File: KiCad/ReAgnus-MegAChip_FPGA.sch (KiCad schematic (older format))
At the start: 2 parts, among them U7 GW1N-UV9LQ144

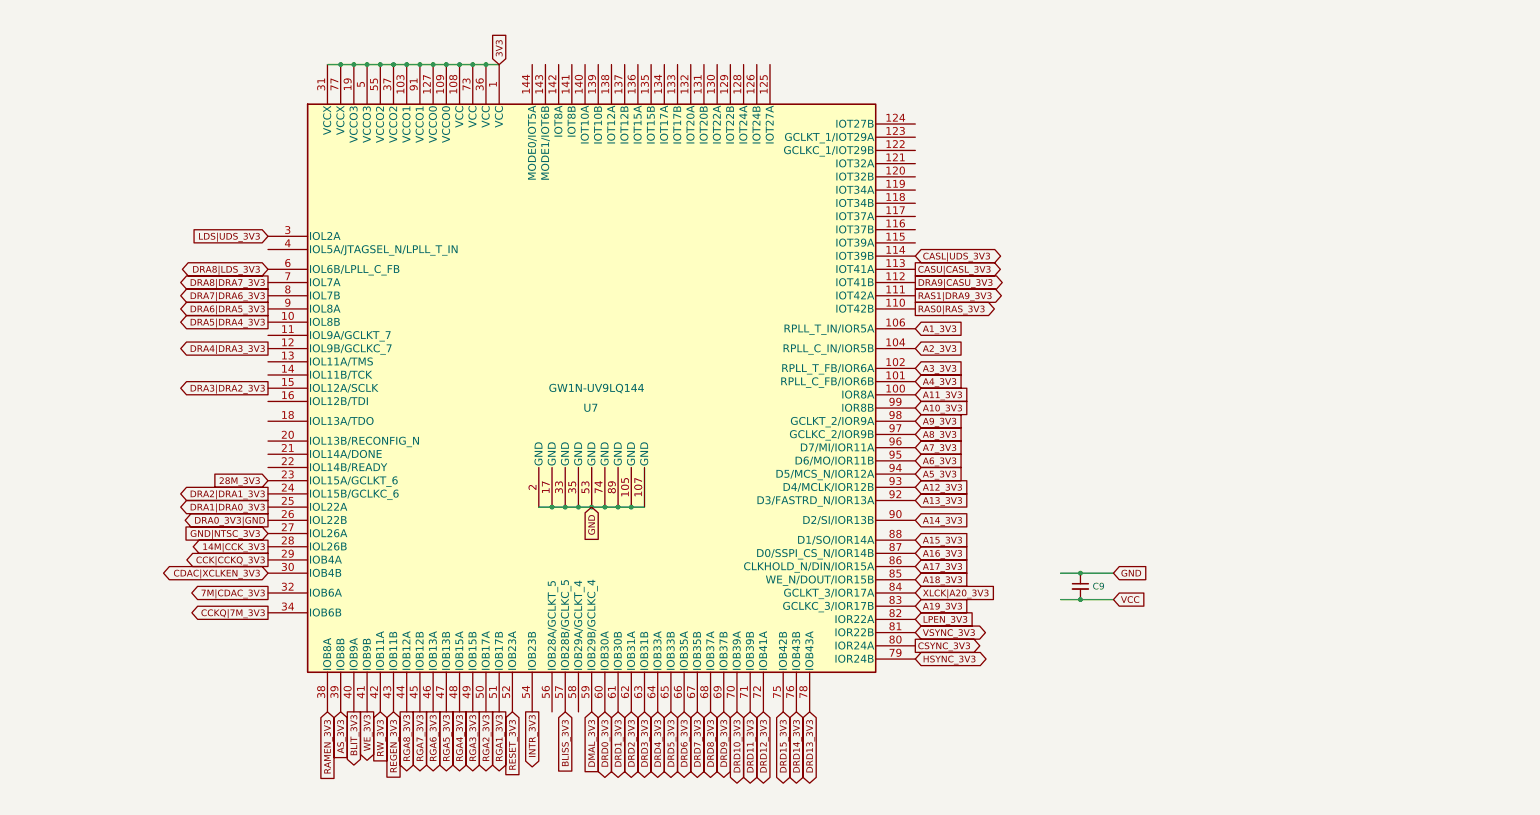
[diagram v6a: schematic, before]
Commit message: added pull-up resistors on PAL/NTSC-line, added JTAG-header
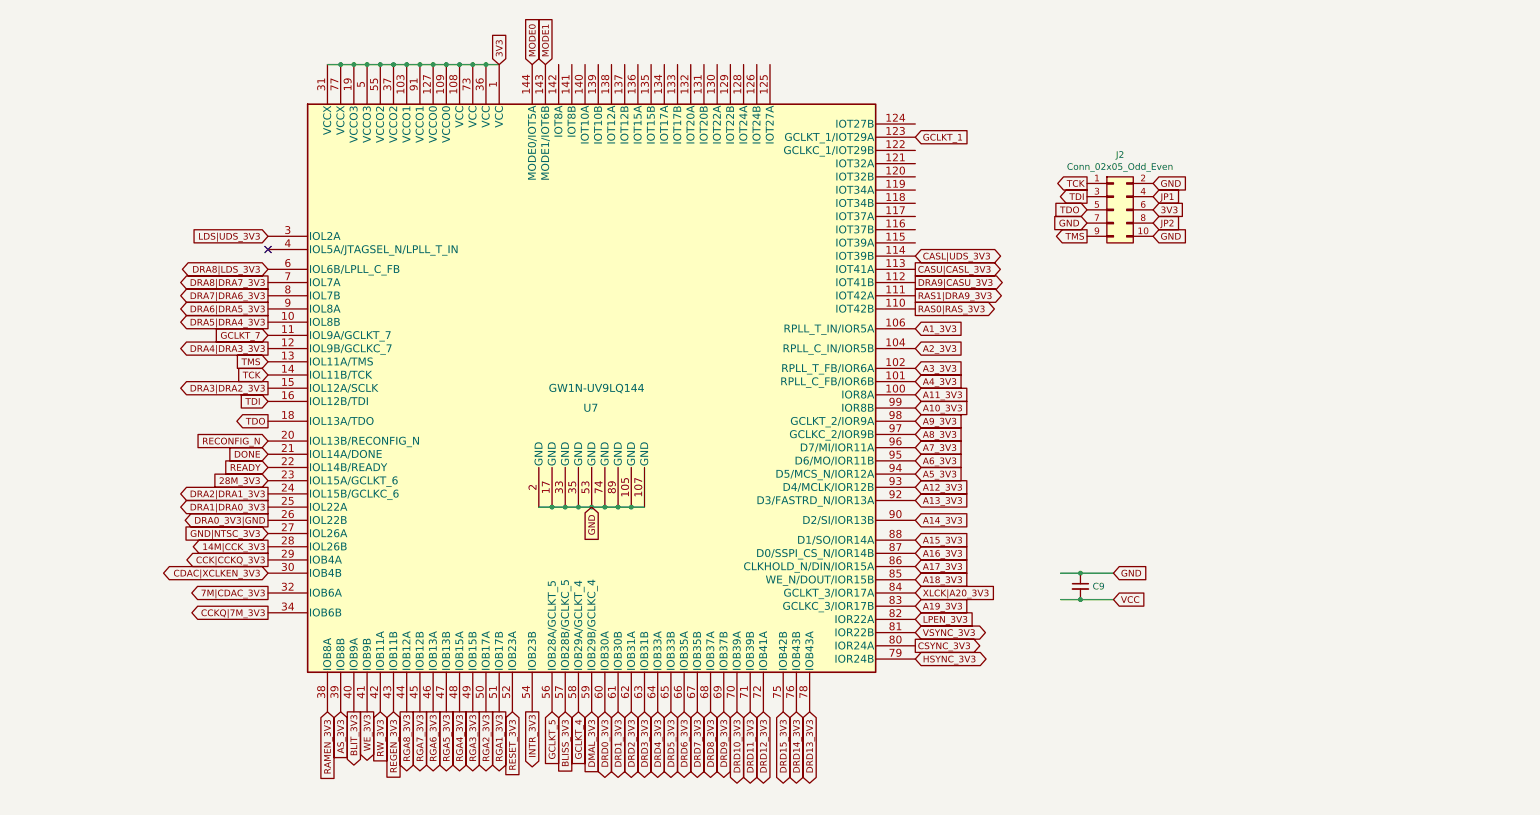
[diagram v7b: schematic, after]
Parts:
- added J2: Conn_02x05_Odd_Even, Connector_PinHeader_2.54mm:PinHeader_2x05_P2.54mm_Vertical, symbol Connector_Generic:Conn_02x05_Odd_Even
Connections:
- net labels added: DONE, GCLKT_1, GCLKT_4, GCLKT_5, GCLKT_7, JP1, JP2, MODE0, MODE1, READY, RECONFIG_N, TCK, TDI, TDO, TMS
- no-connect marks 0 -> 1
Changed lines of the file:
@@
 Text GLabel 3700 5950 3    50   Input ~ 0
 BLISS_3V3
+$Comp
+L Connector_Generic:Conn_02x05_Odd_Even J2
+U 1 1 6329A00B
+P 7850 2150
+F 0 "J2" H 7900 2567 50  0000 C CNN
+F 1 "Conn_02x05_Odd_Even" H 7900 2476 50  0000 C CNN
+F 2 "Connector_PinHeader_2.54mm:PinHeader_2x05_P2.54mm_Vertical" H 7850 2150 50  0001 C CNN
+F 3 "~" H 7850 2150 50  0001 C CNN
+	1    7850 2150
+	1    0    0    -1
+$EndComp
+Text GLabel 7650 1950 0    50   Output ~ 0
+TCK
+Text GLabel 7650 2050 0    50   Output ~ 0
+TDI
+Text GLabel 7650 2150 0    50   Input ~ 0
+TDO
+Text GLabel 7650 2250 0    50   Input ~ 0
+GND
+Text GLabel 7650 2350 0    50   Output ~ 0
+TMS
+Text GLabel 8150 1950 2    50   Input ~ 0
+GND
+Text GLabel 8150 2350 2    50   Input ~ 0
+GND
+Text GLabel 8150 2050 2    50   Input ~ 0
+JP1
+Text GLabel 8150 2250 2    50   Input ~ 0
+JP2
+Text GLabel 8150 2150 2    50   Input ~ 0
+3V3
+Text GLabel 1450 3400 0    50   Input ~ 0
+TCK
+Text GLabel 1450 3600 0    50   Input ~ 0
+TDI
+Text GLabel 1450 3750 0    50   Output ~ 0
+TDO
+Text GLabel 1450 3300 0    50   Input ~ 0
+TMS
+Text GLabel 1450 3900 0    50   Input ~ 0
+RECONFIG_N
+Text GLabel 1450 4000 0    50   Input ~ 0
+DONE
+Text GLabel 1450 4100 0    50   Input ~ 0
+READY
+Text GLabel 1450 3100 0    50   Input ~ 0
+GCLKT_7
+Text GLabel 3600 5950 3    50   Input ~ 0
+GCLKT_5
+Text GLabel 3800 5950 3    50   Input ~ 0
+GCLKT_4
+Text GLabel 6350 1600 2    50   Input ~ 0
+GCLKT_1
+Text GLabel 3550 1050 1    50   Input ~ 0
+MODE1
+Text GLabel 3450 1050 1    50   Input ~ 0
+MODE0
+NoConn ~ 1450 2450
 $EndSCHEMATC

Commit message: more routing and placing components
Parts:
- removed C9: C_Small, Capacitor_SMD:C_1206_3216Metric_Pad1.42x1.75mm_HandSolder, symbol Device:C_Small
- added U10: AS4C4M16SA, Package_SO:TSOP-II-54_22.2x10.16mm_P0.8mm, symbol Memory_RAM:AS4C4M16SA
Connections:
- net labels removed: VCC
- wire segments 25 -> 33
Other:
- moved on the sheet: J2
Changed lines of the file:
@@
 Comment4 ""
 $EndDescr
-Text GLabel 7850 5100 2    50   Input ~ 0
-VCC
-Text GLabel 7850 4900 2    50   Input ~ 0
-GND
 Text GLabel 3900 4400 3    50   Input ~ 0
 GND
-$Comp
-L Device:C_Small C?
-U 1 1 632F85C6
-P 7600 5000
-AR Path="/632F85C6" Ref="C?"  Part="1"
-AR Path="/632D3BDF/632F85C6" Ref="C?"  Part="1"
-AR Path="/632F104D/632F85C6" Ref="C9"  Part="1"
-F 0 "C9" H 7692 5000 50  0000 L CNN
-F 1 "C_Small" H 7692 4955 50  0001 L CNN
-F 2 "Capacitor_SMD:C_1206_3216Metric_Pad1.42x1.75mm_HandSolder" H 7600 5000 50  0001 C CNN
-F 3 "~" H 7600 5000 50  0001 C CNN
-	1    7600 5000
-	1    0    0    -1
-$EndComp
-Wire Wire Line
-	7450 4900 7600 4900
-Connection ~ 7600 4900
-Wire Wire Line
-	7600 4900 7850 4900
-Wire Wire Line
-	7450 5100 7600 5100
-Connection ~ 7600 5100
-Wire Wire Line
-	7600 5100 7850 5100
 Text GLabel 3200 1050 1    50   Input ~ 0
 3V3
@@
 L Connector_Generic:Conn_02x05_Odd_Even J2
 U 1 1 6329A00B
-P 7850 2150
-F 0 "J2" H 7900 2567 50  0000 C CNN
-F 1 "Conn_02x05_Odd_Even" H 7900 2476 50  0000 C CNN
-F 2 "Connector_PinHeader_2.54mm:PinHeader_2x05_P2.54mm_Vertical" H 7850 2150 50  0001 C CNN
-F 3 "~" H 7850 2150 50  0001 C CNN
-	1    7850 2150
+P 7800 1700
+F 0 "J2" H 7850 2117 50  0000 C CNN
+F 1 "Conn_02x05_Odd_Even" H 7850 2026 50  0000 C CNN
+F 2 "Connector_PinHeader_2.54mm:PinHeader_2x05_P2.54mm_Vertical" H 7800 1700 50  0001 C CNN
+F 3 "~" H 7800 1700 50  0001 C CNN
+	1    7800 1700
 	1    0    0    -1
 $EndComp
-Text GLabel 7650 1950 0    50   Output ~ 0
+Text GLabel 7600 1500 0    50   Output ~ 0
 TCK
-Text GLabel 7650 2050 0    50   Output ~ 0
+Text GLabel 7600 1600 0    50   Output ~ 0
 TDI
-Text GLabel 7650 2150 0    50   Input ~ 0
+Text GLabel 7600 1700 0    50   Input ~ 0
 TDO
-Text GLabel 7650 2250 0    50   Input ~ 0
-GND
-Text GLabel 7650 2350 0    50   Output ~ 0
+Text GLabel 7600 1800 0    50   Input ~ 0
+GND
+Text GLabel 7600 1900 0    50   Output ~ 0
 TMS
-Text GLabel 8150 1950 2    50   Input ~ 0
-GND
-Text GLabel 8150 2350 2    50   Input ~ 0
-GND
-Text GLabel 8150 2050 2    50   Input ~ 0
+Text GLabel 8100 1500 2    50   Input ~ 0
+GND
+Text GLabel 8100 1900 2    50   Input ~ 0
+GND
+Text GLabel 8100 1600 2    50   Input ~ 0
 JP1
-Text GLabel 8150 2250 2    50   Input ~ 0
+Text GLabel 8100 1800 2    50   Input ~ 0
 JP2
-Text GLabel 8150 2150 2    50   Input ~ 0
+Text GLabel 8100 1700 2    50   Input ~ 0
 3V3
 Text GLabel 1450 3400 0    50   Input ~ 0
@@
 MODE0
 NoConn ~ 1450 2450
+$Comp
+L Memory_RAM:AS4C4M16SA U10
+U 1 1 632B4228
+P 9150 3700
+F 0 "U10" H 9150 5181 50  0000 C CNN
+F 1 "AS4C4M16SA" H 9150 5090 50  0000 C CNN
+F 2 "Package_SO:TSOP-II-54_22.2x10.16mm_P0.8mm" H 9150 3700 50  0001 C CIN
+F 3 "https://www.alliancememory.com/wp-content/uploads/pdf/dram/64M-AS4C4M16SA-CI_v3.0_March%202015.pdf" H 9150 3450 50  0001 C CNN
+	1    9150 3700
+	1    0    0    -1
+$EndComp
+Text GLabel 9950 4150 2    50   BiDi ~ 0
+DRD0_3V3
+Text GLabel 9950 4050 2    50   BiDi ~ 0
+DRD1_3V3
+Text GLabel 9950 3950 2    50   BiDi ~ 0
+DRD2_3V3
+Text GLabel 9950 3850 2    50   BiDi ~ 0
+DRD3_3V3
+Text GLabel 9950 3750 2    50   BiDi ~ 0
+DRD4_3V3
+Text GLabel 9950 3650 2    50   BiDi ~ 0
+DRD5_3V3
+Text GLabel 9950 3550 2    50   BiDi ~ 0
+DRD6_3V3
+Text GLabel 9950 3450 2    50   BiDi ~ 0
+DRD7_3V3
+Text GLabel 9950 3350 2    50   BiDi ~ 0
+DRD8_3V3
+Text GLabel 9950 2650 2    50   BiDi ~ 0
+DRD9_3V3
+Text GLabel 9950 2750 2    50   BiDi ~ 0
+DRD10_3V3
+Text GLabel 9950 2850 2    50   BiDi ~ 0
+DRD11_3V3
+Text GLabel 9950 2950 2    50   BiDi ~ 0
+DRD12_3V3
+Text GLabel 9950 3050 2    50   BiDi ~ 0
+DRD13_3V3
+Text GLabel 9950 3150 2    50   BiDi ~ 0
+DRD14_3V3
+Text GLabel 9950 3250 2    50   BiDi ~ 0
+DRD15_3V3
+Text GLabel 8850 2400 1    50   Input ~ 0
+3V3
+Wire Wire Line
+	8850 2400 8950 2400
+Connection ~ 8950 2400
+Wire Wire Line
+	8950 2400 9050 2400
+Connection ~ 9050 2400
+Wire Wire Line
+	9050 2400 9150 2400
+Connection ~ 9150 2400
+Wire Wire Line
+	9150 2400 9250 2400
+Connection ~ 9250 2400
+Wire Wire Line
+	9250 2400 9350 2400
+Connection ~ 9350 2400
+Wire Wire Line
+	9350 2400 9450 2400
+Text GLabel 8850 5000 3    50   Input ~ 0
+GND
+Wire Wire Line
+	8850 5000 8950 5000
+Connection ~ 8950 5000
+Wire Wire Line
+	8950 5000 9050 5000
+Connection ~ 9050 5000
+Wire Wire Line
+	9050 5000 9150 5000
+Connection ~ 9150 5000
+Wire Wire Line
+	9150 5000 9250 5000
+Connection ~ 9250 5000
+Wire Wire Line
+	9250 5000 9350 5000
+Connection ~ 9350 5000
+Wire Wire Line
+	9350 5000 9450 5000
 $EndSCHEMATC
